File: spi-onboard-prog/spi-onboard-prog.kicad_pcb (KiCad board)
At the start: 2 copper layers, 46 parts, among them CN1 USERPORT-C64-CONN, IC1 74LS07, IC4 74164DLS, J3 USB_C_Receptacle_USB2.0_16P, P2 PETUSERPORT, Q3 12MHz, U1 SST25VF080B-50-4x-S2Ax, U2 CH341A, U3 74LS257

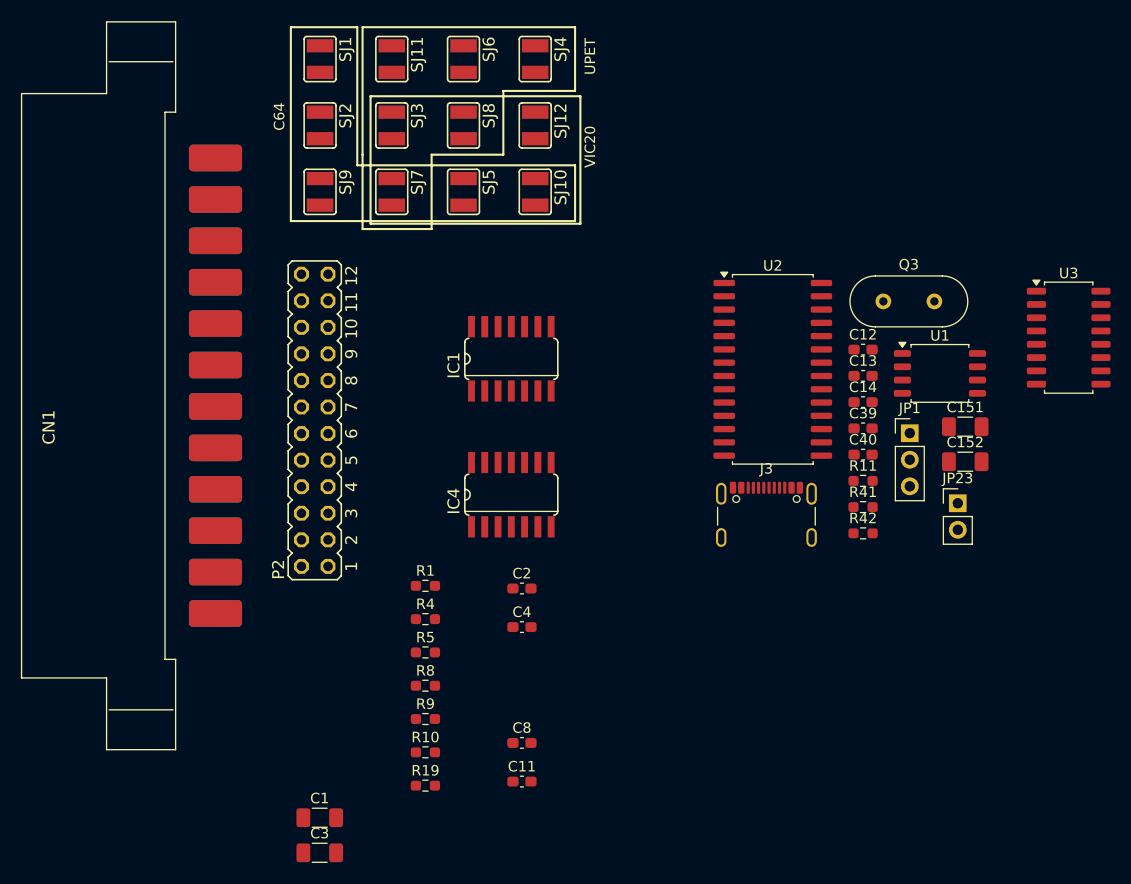
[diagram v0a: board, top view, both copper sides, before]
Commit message: layout work on onboard spi prog
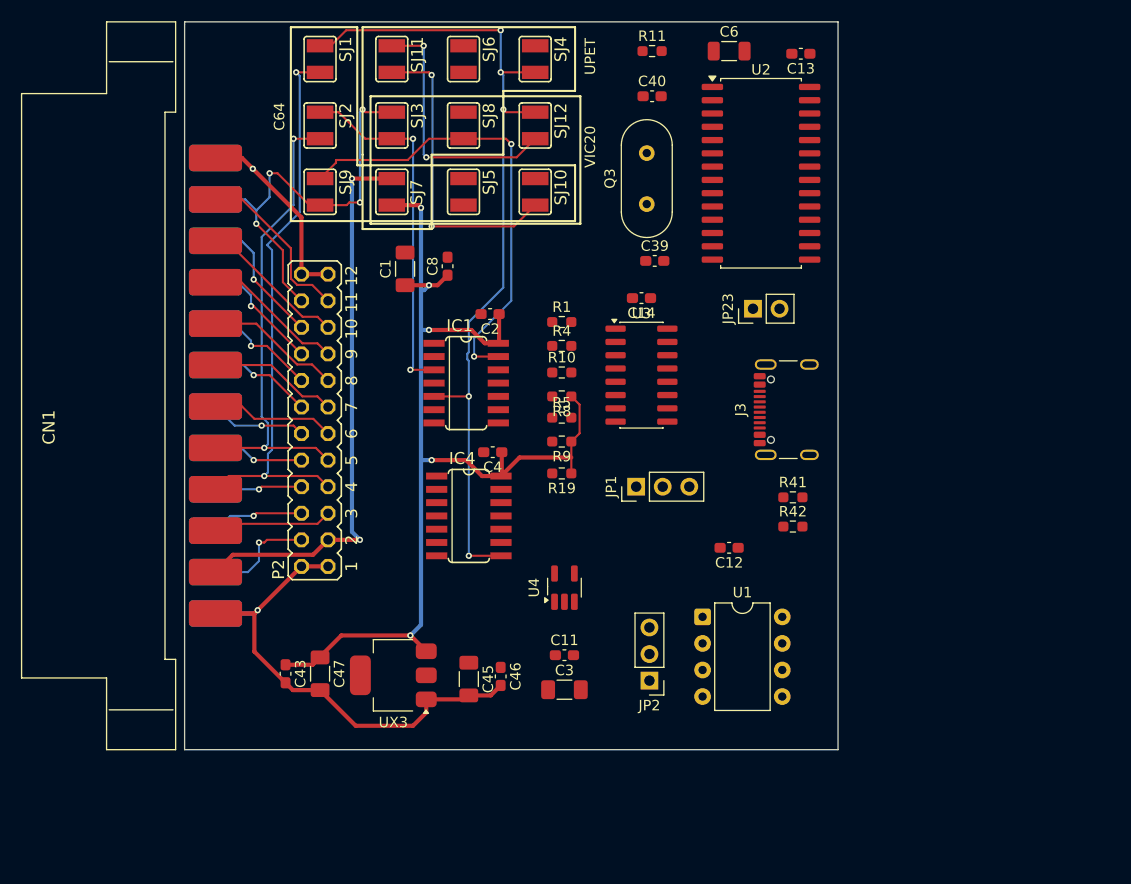
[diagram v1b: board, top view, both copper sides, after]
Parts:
- removed C151, C152: 47u, Capacitor_SMD:C_1206_3216Metric_Pad1.33x1.80mm_HandSolder
- added C43: 100n, Capacitor_SMD:C_0603_1608Metric_Pad1.08x0.95mm_HandSolder, F.Cu at (93.2, 131.9)
- added C45: 22u, Capacitor_SMD:C_1206_3216Metric_Pad1.33x1.80mm_HandSolder, F.Cu at (110.7, 132.4)
- added C46: 100n, Capacitor_SMD:C_0603_1608Metric_Pad1.08x0.95mm_HandSolder, F.Cu at (113.8, 132.2)
- added C47: 22u, Capacitor_SMD:C_1206_3216Metric_Pad1.33x1.80mm_HandSolder, F.Cu at (96.5, 131.9)
- added C6: 47u, Capacitor_SMD:C_1206_3216Metric, F.Cu at (135.6, 72.4)
- added JP2: Jumper_3_Open, Connector_PinHeader_2.54mm:PinHeader_1x03_P2.54mm_Vertical, F.Cu at (128.0, 132.6)
- added U4: 74LVC1G125, Package_TO_SOT_SMD:SOT-23-5_HandSoldering, F.Cu at (119.9, 123.7)
- added UX3: LDI1117, Package_TO_SOT_SMD:SOT-223, F.Cu at (103.5, 132.1)
- U1: footprint Package_SO:SOIC-8_5.3x5.3mm_P1.27mm -> Package_DIP:DIP-8_W7.62mm
- U3: value 74LS257 -> 74LVC257; footprint Package_SO:SOP-16_4.4x10.4mm_P1.27mm -> Package_SO:SOIC-16_3.9x9.9mm_P1.27mm
- moved C1 53.1 mm to (104.6, 93.2), turned to 90 degrees
- moved C8 46.1 mm to (108.7, 93.0), turned to 90 degrees
- moved R11 45.8 mm to (128.3, 72.4)
- moved U3 41.0 mm to (127.3, 103.4)
- moved C40 39.8 mm to (128.3, 76.7)
- moved R10 38.6 mm to (119.6, 103.1)
- moved R19 32.6 mm to (119.6, 112.8), turned to 180 degrees
- moved U1 32.5 mm to (133.1, 126.5)
- moved C13 31.4 mm to (142.5, 72.6), turned to 180 degrees
- moved R8 30.6 mm to (119.6, 105.4), turned to 180 degrees
- moved R9 29.6 mm to (119.6, 109.7), turned to 180 degrees
- moved R4 29.2 mm to (119.6, 100.6)
- moved R1 28.4 mm to (119.6, 98.3)
- moved C3 28.1 mm to (119.9, 133.5)
- moved JP23 27.0 mm to (137.9, 97.0), turned to 90 degrees
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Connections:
- C1 pad 1: VCC -> 5V
- C2 pad 1: VCC -> 5V
- C4 pad 1: VCC -> 5V
- C8 pad 1: VCC -> 5V
- IC1 pad 14: (no net) -> 5V
- IC1 pad 7: (no net) -> GND
- IC4 pad 14: (no net) -> 5V
- IC4 pad 7: (no net) -> GND
- R19 pad 1: VCC -> 5V
- R8 pad 1: VCC -> 5V
- R9 pad 1: VCC -> 5V
- SJ7 pad 1: VCC -> 5V
- U1 pad 2: unconnected-(U1-SO-Pad2) -> MISO2
- U3 pad 1: unconnected-(U3-S-Pad1) -> Net-(JP2-C)
- U3 pad 15: unconnected-(U3-OE-Pad15) -> GND
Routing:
- net 5V: track 0.00 -> 101.7 mm, vias 0 -> 5
- net SPICLK: track 0.00 -> 82.6 mm, vias 0 -> 5
- net GND: track 0.00 -> 69.9 mm, vias 0 -> 2
- net C64CLK: track 0.00 -> 54.6 mm, vias 0 -> 2
- net Net-(CN1-VCC): track 0.00 -> 53.8 mm, vias 0 -> 2
- net C64DATA: track 0.00 -> 45.0 mm, vias 0 -> 2
- net /SPISEL: track 0.00 -> 44.3 mm, vias 0 -> 2
- net PETVICDATA/C64SEL: track 0.00 -> 40.7 mm, vias 0 -> 4
- net /PETINT/VICCLK: track 0.00 -> 35.5 mm, vias 0 -> 3
- net SPIMOSI: track 0.00 -> 34.4 mm, vias 0 -> 2
- net /SPIINT: track 0.00 -> 29.2 mm, vias 0 -> 2
- net Net-(CN1-9VAC2): track 0.00 -> 16.5 mm
- net Net-(CN1-9VAC1): track 0.00 -> 14.2 mm
- net Net-(CN1-ATN): track 0.00 -> 13.6 mm
- net IND7: track 0.00 -> 13.1 mm, vias 0 -> 1
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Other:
- board outline added: 62.5 x 69.6 mm

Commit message: move spi onboard prog to draft spi userport
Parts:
- added C48: 22u, Capacitor_SMD:C_1206_3216Metric_Pad1.33x1.80mm_HandSolder, F.Cu at (113.0, 135.4)
- added P3: CBMTAPE, Connector_PinHeader_2.54mm:PinHeader_1x06_P2.54mm_Vertical, F.Cu at (94.2, 136.4)
- moved C45 3.64 mm to (110.0, 128.9)
- moved C46 3.64 mm to (113.0, 128.6)
- moved UX3 3.64 mm to (102.8, 128.5)
- moved C47 3.64 mm to (95.8, 128.4)
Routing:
- net 5V: track 101.7 -> 101.0 mm
- net GND: track 69.9 -> 70.6 mm

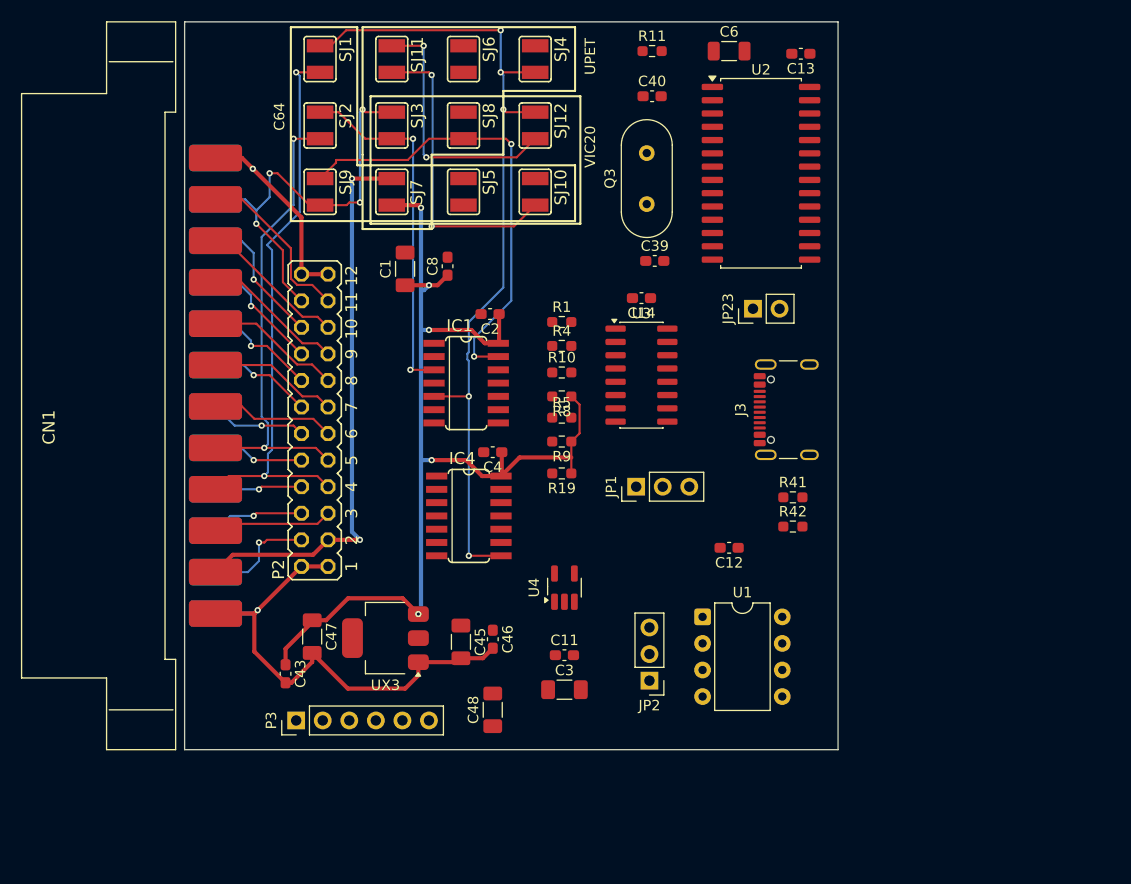
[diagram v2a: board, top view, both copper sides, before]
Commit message: onboard prog on SPI10-3.3V
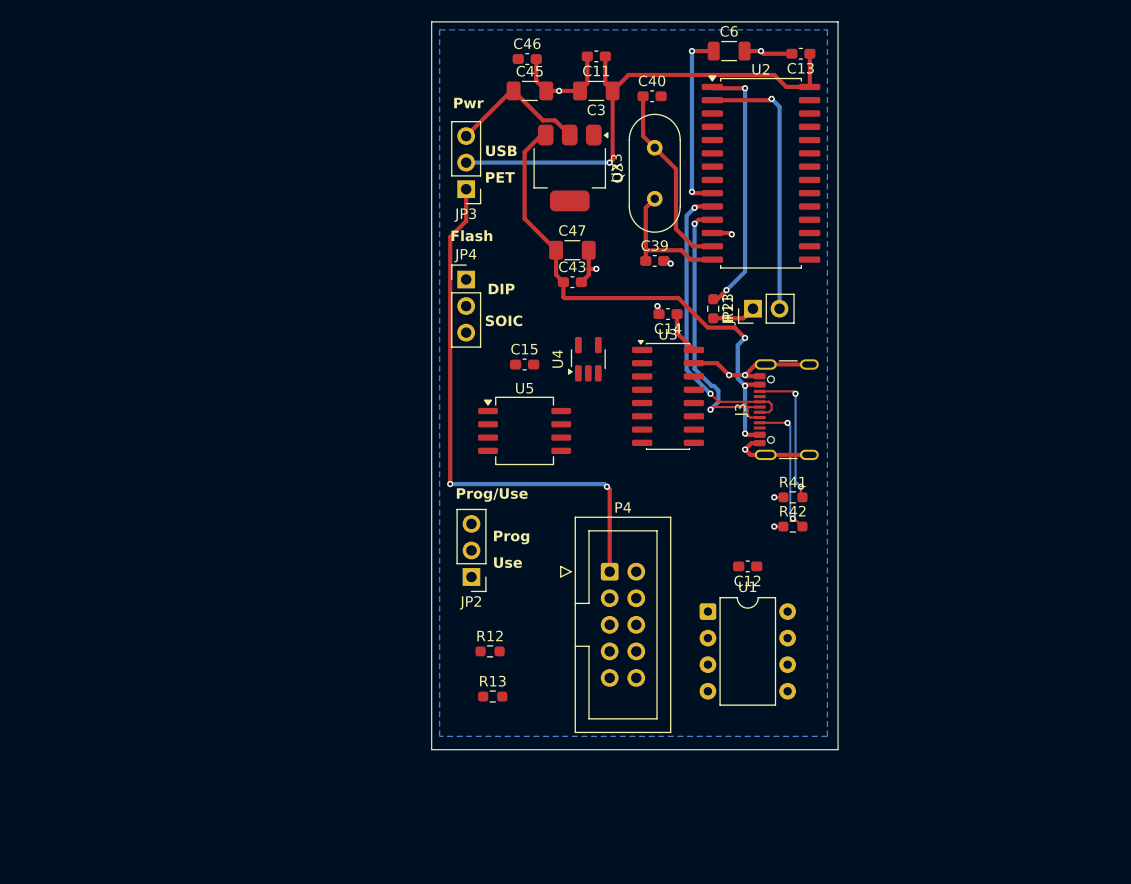
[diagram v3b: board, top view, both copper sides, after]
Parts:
- removed C1: C_Polarized, Capacitor_SMD:C_1206_3216Metric_Pad1.33x1.80mm_HandSolder
- removed C2, C4, C8: 100n, Capacitor_SMD:C_0603_1608Metric_Pad1.08x0.95mm_HandSolder
- removed C48: 22u, Capacitor_SMD:C_1206_3216Metric_Pad1.33x1.80mm_HandSolder
- removed CN1: USERPORT-C64-CONN, cbm_usb_v1-import-fps:UPS24CONN
- removed IC1: 74LS07, cbm_usb_v1-import-fps:SO14
- removed IC4: 74164DLS, cbm_usb_v1-import-fps:SO14
- removed JP1: Jumper_3_Open, Connector_PinHeader_2.54mm:PinHeader_1x03_P2.54mm_Vertical
- removed P2: PETUSERPORT, cbm_usb_v1-import-fps:FLAT24
- removed P3: CBMTAPE, Connector_PinHeader_2.54mm:PinHeader_1x06_P2.54mm_Vertical
- removed R1, R10, R19, R4, R5, R8, R9: 3k3, Resistor_SMD:R_0603_1608Metric_Pad0.98x0.95mm_HandSolder
- removed SJ1, SJ10, SJ11, SJ12, SJ2, SJ3, SJ4, SJ5, SJ6, SJ7, SJ8, SJ9: SJW, cbm_usb_v1-import-fps:SJW
- added C15: 100n, Capacitor_SMD:C_0603_1608Metric_Pad1.08x0.95mm_HandSolder, F.Cu at (116.1, 102.4)
- added JP3: Jumper_3_Open, Connector_PinHeader_2.54mm:PinHeader_1x03_P2.54mm_Vertical, F.Cu at (110.5, 85.6)
- added JP4: Jumper_3_Open, Connector_PinHeader_2.54mm:PinHeader_1x03_P2.54mm_Vertical, F.Cu at (110.5, 94.2)
- added P4: ~, Connector_IDC:IDC-Header_2x05_P2.54mm_Vertical, F.Cu at (124.2, 122.2)
- added R12: 47k, Resistor_SMD:R_0603_1608Metric_Pad0.98x0.95mm_HandSolder, F.Cu at (112.8, 129.8)
- added R13: 47k, Resistor_SMD:R_0603_1608Metric_Pad0.98x0.95mm_HandSolder, F.Cu at (113.0, 134.1)
- added U5: SST25VF080B-50-4x-S2Ax, Package_SO:SOIC-8_5.3x6.2mm_P1.27mm, F.Cu at (116.1, 108.7)
- moved C11 57.3 mm to (122.9, 72.9), turned to 180 degrees
- moved C3 57.3 mm to (122.9, 76.2), turned to 180 degrees
- moved C46 55.6 mm to (116.3, 73.2), turned to 0 degrees
- moved C45 53.1 mm to (116.6, 76.2), turned to 0 degrees
- moved UX3 48.3 mm to (120.4, 83.6), turned to -90 degrees
- moved C43 46.4 mm to (120.7, 94.5), turned to 0 degrees
- moved C47 44.5 mm to (120.7, 91.4), turned to 0 degrees
- moved R11 25.3 mm to (134.1, 97.0), turned to -90 degrees
- moved U4 22.0 mm to (122.2, 101.9)
- moved JP2 19.7 mm to (111.0, 122.7)
- moved U3 3.25 mm to (129.8, 105.4)
- moved C14 2.96 mm to (129.8, 97.5)
- moved C12 2.51 mm to (137.4, 121.7)
- moved Q3 0.92 mm to (128.5, 86.5)
- moved U1 0.72 mm to (133.6, 126.0)
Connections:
- C45 pad 1: 3.3V -> Net-(JP3-B)
- C46 pad 1: 3.3V -> Net-(JP3-B)
- J3 pad A4: VCCIN -> 5V
- J3 pad A9: VCCIN -> 5V
- J3 pad B4: VCCIN -> 5V
- J3 pad B9: VCCIN -> 5V
- J3 pad SH: (no net) -> GND
- U1 pad 3: unconnected-(U1-~{WP}-Pad3) -> 3.3V
- U1 pad 7: unconnected-(U1-~{HOLD}-Pad7) -> 3.3V
- U2 pad 15: Net-(JP1-B) -> USB_CS0
- U2 pad 16: Net-(JP1-A) -> USB_CS1
- U3 pad 10: unconnected-(U3-I1d-Pad10) -> USB_CS1
- U3 pad 11: unconnected-(U3-I0d-Pad11) -> Net-(JP4-B)
- U3 pad 2: /SS2 -> Net-(JP4-A)
- U3 pad 3: USB_CS -> USB_CS0
- U3 pad 9: unconnected-(U3-Zd-Pad9) -> Net-(U3-Zd)
- UX3 pad 2: 3.3V -> Net-(JP3-B)
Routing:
- net SPICLK: track 82.6 -> 0.00 mm, vias 5 -> 0
- net C64CLK: track 54.6 -> 0.00 mm, vias 2 -> 0
- net Net-(CN1-VCC): track 53.8 -> 0.00 mm, vias 2 -> 0
- net Net-(JP3-A): track 0.00 -> 52.2 mm, vias 0 -> 2
- net 3.3V: track 0.00 -> 51.5 mm, vias 0 -> 1
- net 5V: track 101.0 -> 49.7 mm, vias 5 -> 3
- net C64DATA: track 45.0 -> 0.00 mm, vias 2 -> 0
- net /SPISEL: track 44.3 -> 0.00 mm, vias 2 -> 0
- net PETVICDATA/C64SEL: track 40.7 -> 0.00 mm, vias 4 -> 0
- net /PETINT/VICCLK: track 35.5 -> 0.00 mm, vias 3 -> 0
- net SPIMOSI: track 34.4 -> 0.00 mm, vias 2 -> 0
- net /SPIINT: track 29.2 -> 0.00 mm, vias 2 -> 0
- net UCD+: track 0.00 -> 28.8 mm, vias 0 -> 2
- net UCD-: track 0.00 -> 27.8 mm, vias 0 -> 2
- net Net-(U2-RSTI): track 0.00 -> 26.1 mm, vias 0 -> 1
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- added copper zone on B.Cu, net GND
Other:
- board size 62.5 x 69.6 mm -> 38.9 x 69.6 mm
- board text added: "DIP"
- board text added: "Flash"
- board text added: "PET"
- board text added: "Prog"
- board text added: "Prog/Use"
- board text added: "Pwr"
- board text added: "SOIC"
- board text added: "USB"
- board text added: "Use"
- board text removed: "C64"
- board text removed: "UPET"
- board text removed: "VIC20"

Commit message: onboard flash prog
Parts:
- added U6: 74LVC1G04, Package_TO_SOT_SMD:SOT-23-5_HandSoldering, F.Cu at (133.1, 114.6)
- C3: value C_Polarized -> 47u
- C45, C47: value 22u -> 47u
- U2: footprint Package_SO:SOIC-28W_7.5x17.9mm_P1.27mm -> Package_SO:SOP-28_8.4x18.16mm_P1.27mm
- moved R13 36.1 mm to (115.1, 98.0), turned to 180 degrees
- moved R12 35.6 mm to (115.1, 94.2), turned to 180 degrees
- moved C15 1.02 mm to (116.1, 103.4), turned to 180 degrees
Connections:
- C6 pad 1: Net-(U2-V3) -> 3.3V
- JP23 pad 2: Net-(U2-RSTI) -> Net-(U2-TNOW/~{INI}/~{RST})
- U2 pad 26: /RES -> Net-(U2-TNOW/~{INI}/~{RST})
- U2 pad 9: Net-(U2-V3) -> 3.3V
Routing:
- net 3.3V: track 51.5 -> 275.8 mm, vias 1 -> 11
- net GND: track 45.6 -> 164.0 mm, vias 11 -> 23
- net Net-(U1-SI): track 0.00 -> 64.3 mm, vias 0 -> 3
- net /SS2: track 0.00 -> 53.2 mm, vias 0 -> 2
- net MISO2: track 0.00 -> 51.7 mm, vias 0 -> 3
- net Net-(U1-SCK): track 0.00 -> 41.9 mm, vias 0 -> 2
- net USB_SCK: track 0.00 -> 38.6 mm, vias 0 -> 2
- net USB_MISO: track 0.00 -> 36.7 mm, vias 0 -> 2
- net Net-(JP2-C): track 0.00 -> 36.0 mm, vias 0 -> 2
- net SCLK: track 0.00 -> 32.8 mm, vias 0 -> 2
- net MOSI: track 0.00 -> 31.7 mm, vias 0 -> 2
- net USB_MOSI: track 0.00 -> 30.5 mm, vias 0 -> 2
- net Net-(JP4-B): track 0.00 -> 30.4 mm, vias 0 -> 2
- net Net-(U3-Zd): track 0.00 -> 28.7 mm
- net Net-(U1-~{CE}): track 0.00 -> 28.1 mm, vias 0 -> 2
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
